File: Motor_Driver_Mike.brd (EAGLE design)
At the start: 127 x 76.2 mm, 88 parts

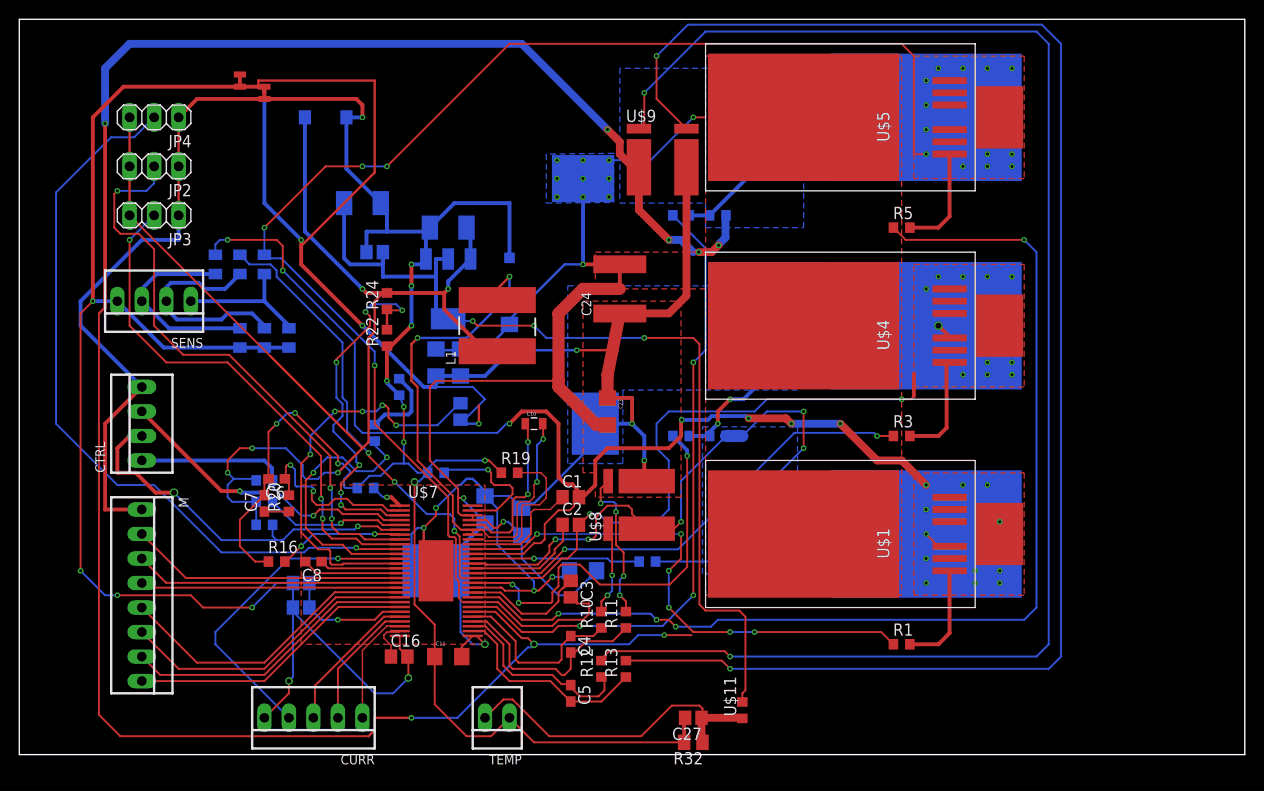
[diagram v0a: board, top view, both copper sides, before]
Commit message: Fixed H1_LOW, H3_LOW traces (made them wider and added a polygon around driver for H1_LOW)
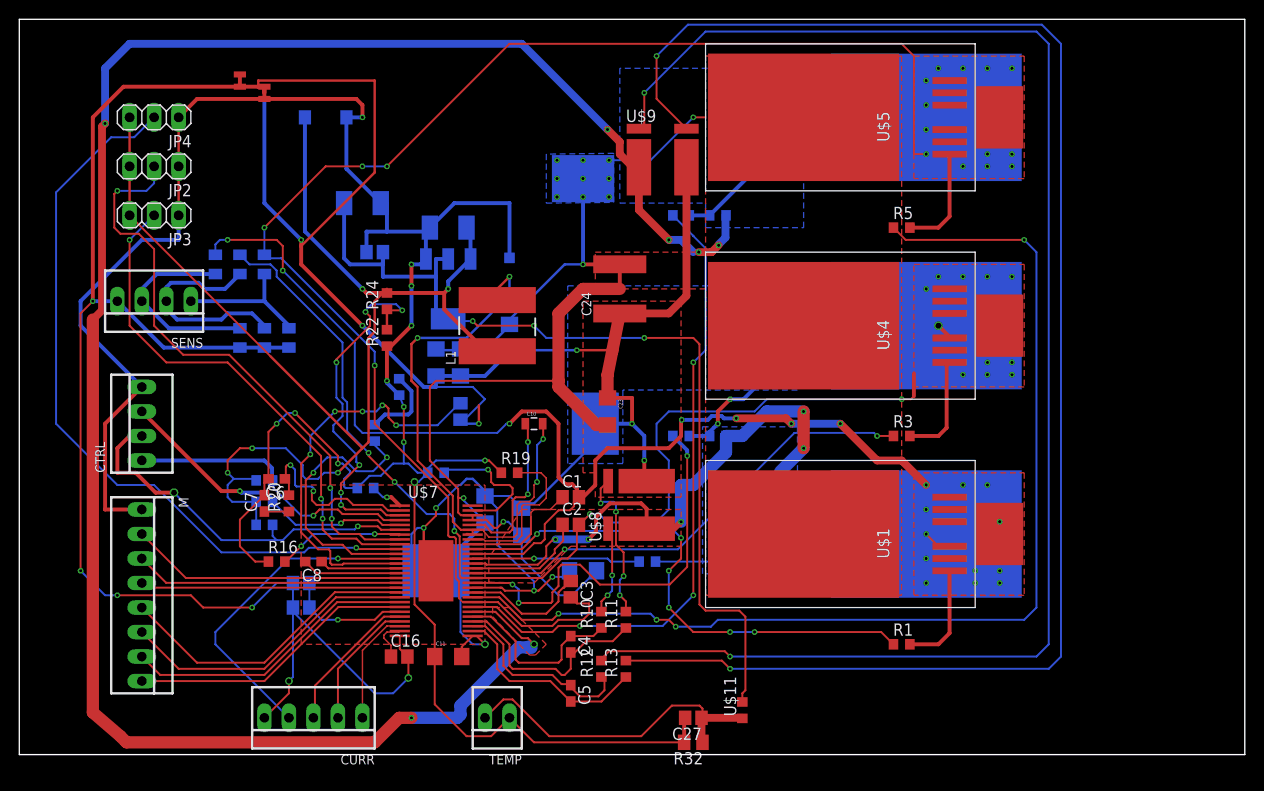
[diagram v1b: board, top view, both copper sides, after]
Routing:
- net H3_LOW: track 223.2 -> 207.4 mm, vias 8 -> 7
- net H1_LOW: track 61.1 -> 63.2 mm
- added copper zone on layer 1, net H1_LOW
- added copper zone on layer 1, net N$9

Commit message: changed board dimensions to get it down to 10 by 10
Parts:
- moved CURR 5.24 mm to (25.4, 5.08)
- moved C27 5.24 mm to (64.8, 5.08)
- moved R32 5.24 mm to (64.8, 2.54)
- moved TEMP 5.24 mm to (44.5, 5.08)
- moved U$11 5.08 mm to (69.8, 4.60)
- moved C10 5.08 mm to (48.3, 34.3)
- moved C11 5.08 mm to (39.4, 10.2)
- moved C9 5.08 mm to (39.4, 54.6)
- moved R10 5.08 mm to (55.2, 14.0)
- moved R11 5.08 mm to (57.8, 14.0)
- moved R12 5.08 mm to (55.2, 8.89)
- moved R13 5.08 mm to (57.8, 8.89)
- moved R2 5.08 mm to (60.0, 20.0)
- moved U$10 5.08 mm to (39.4, 48.3)
- moved U$8 5.08 mm to (59.1, 25.9)
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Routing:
- net GAIN: track 78.7 -> 105.9 mm, vias 1 -> 5
- net N$128: track 162.4 -> 158.9 mm
- net TEMP: track 34.2 -> 37.6 mm
- net N$124: track 158.9 -> 156.3 mm
- net DC_CAL: track 34.3 -> 32.0 mm
- net DGND: track 250.5 -> 252.8 mm
- net H3_LOW: track 207.4 -> 208.9 mm
- net AGND: track 147.1 -> 145.8 mm
- net SO2: track 11.9 -> 10.7 mm
- net SO1: track 13.5 -> 12.3 mm
- net REF: track 15.2 -> 16.1 mm
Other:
- board size 127 x 76.2 mm -> 101.6 x 76.2 mm
